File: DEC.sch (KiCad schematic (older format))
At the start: 4 parts

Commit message: wiring
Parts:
- gave numbers to parts that had none: 4
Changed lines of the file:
@@
 $Descr A4 11693 8268
 encoding utf-8
-Sheet 8 8
+Sheet 8 20
 Title ""
 Date ""
@@
 Z7
 $Comp
-L 74LS283 U?
+L 74LS283 U11
 U 1 1 5AE75C93
 P 3050 4250
-F 0 "U?" H 3050 4250 50  0000 C CNN
+F 0 "U11" H 3050 4250 50  0000 C CNN
 F 1 "74LS283" H 3100 3900 50  0000 C CNN
 F 2 "" H 3050 4250 50  0000 C CNN
@@
 $EndComp
 $Comp
-L 74LS283 U?
+L 74LS283 U12
 U 1 1 5AE75D41
 P 4625 4350
-F 0 "U?" H 4625 4350 50  0000 C CNN
+F 0 "U12" H 4625 4350 50  0000 C CNN
 F 1 "74LS283" H 4675 4000 50  0000 C CNN
 F 2 "" H 4625 4350 50  0000 C CNN
@@
 	4625 3100 4625 3650
 $Comp
-L VCC #PWR?
+L VCC #PWR14
 U 1 1 5AE760F6
 P 3375 5400
-F 0 "#PWR?" H 3375 5250 50  0001 C CNN
+F 0 "#PWR14" H 3375 5250 50  0001 C CNN
 F 1 "VCC" H 3375 5550 50  0000 C CNN
 F 2 "" H 3375 5400 50  0000 C CNN
@@
 $EndComp
 $Comp
-L VCC #PWR?
+L VCC #PWR15
 U 1 1 5AE7610E
 P 5025 5400
-F 0 "#PWR?" H 5025 5250 50  0001 C CNN
+F 0 "#PWR15" H 5025 5250 50  0001 C CNN
 F 1 "VCC" H 5025 5550 50  0000 C CNN
 F 2 "" H 5025 5400 50  0000 C CNN
@@
 	5075 5050 4975 5050
 $Comp
-L VCC #PWR?
+L VCC #PWR13
 U 1 1 5AE7639B
 P 2075 3750
-F 0 "#PWR?" H 2075 3600 50  0001 C CNN
+F 0 "#PWR13" H 2075 3600 50  0001 C CNN
 F 1 "VCC" H 2075 3900 50  0000 C CNN
 F 2 "" H 2075 3750 50  0000 C CNN
@@
 $EndComp
 $Comp
-L GND #PWR?
+L GND #PWR12
 U 1 1 5AE763B3
 P 2050 4500
-F 0 "#PWR?" H 2050 4250 50  0001 C CNN
+F 0 "#PWR12" H 2050 4250 50  0001 C CNN
 F 1 "GND" H 2050 4350 50  0000 C CNN
 F 2 "" H 2050 4500 50  0000 C CNN
@@
 $EndComp
 $Comp
-L GND #PWR?
+L GND #PWR16
 U 1 1 5AE763CB
 P 5600 3900
-F 0 "#PWR?" H 5600 3650 50  0001 C CNN
+F 0 "#PWR16" H 5600 3650 50  0001 C CNN
 F 1 "GND" H 5600 3750 50  0000 C CNN
 F 2 "" H 5600 3900 50  0000 C CNN
@@
 	2400 4950 2600 4950
 $Comp
-L C_Small C?
+L C_Small C5
 U 1 1 5AE7641F
 P 2025 4075
-F 0 "C?" H 2035 4145 50  0000 L CNN
+F 0 "C5" H 2035 4145 50  0000 L CNN
 F 1 "100n" H 2035 3995 50  0000 L CNN
 F 2 "" H 2025 4075 50  0000 C CNN
@@
 $EndComp
 $Comp
-L C_Small C?
+L C_Small C6
 U 1 1 5AE76480
 P 5375 4375
-F 0 "C?" H 5385 4445 50  0000 L CNN
+F 0 "C6" H 5385 4445 50  0000 L CNN
 F 1 "100n" H 5385 4295 50  0000 L CNN
 F 2 "" H 5375 4375 50  0000 C CNN

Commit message: SPICE capacitance and ground symbols
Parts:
- removed C5, C6: 100n, symbol C_Small
- added C? (x2): C, symbol C
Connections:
- net labels added: 0
- net labels removed: GND
- wire segments 58 -> 61
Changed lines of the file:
@@
 EESchema Schematic File Version 2
-LIBS:power
-LIBS:device
-LIBS:transistors
-LIBS:conn
-LIBS:linear
-LIBS:regul
-LIBS:74xx
-LIBS:cmos4000
-LIBS:adc-dac
-LIBS:memory
-LIBS:xilinx
-LIBS:microcontrollers
-LIBS:dsp
-LIBS:microchip
-LIBS:analog_switches
-LIBS:motorola
-LIBS:texas
-LIBS:intel
-LIBS:audio
-LIBS:interface
-LIBS:digital-audio
-LIBS:philips
-LIBS:display
-LIBS:cypress
-LIBS:siliconi
-LIBS:opto
-LIBS:atmel
-LIBS:contrib
-LIBS:valves
+LIBS:spice
+LIBS:pspice
 LIBS:myCpu-cache
 EELAYER 25 0
@@
 L VCC #PWR15
 U 1 1 5AE7610E
-P 5025 5400
-F 0 "#PWR15" H 5025 5250 50  0001 C CNN
-F 1 "VCC" H 5025 5550 50  0000 C CNN
-F 2 "" H 5025 5400 50  0000 C CNN
-F 3 "" H 5025 5400 50  0000 C CNN
-	1    5025 5400
+P 4925 5400
+F 0 "#PWR15" H 4925 5250 50  0001 C CNN
+F 1 "VCC" H 4925 5550 50  0000 C CNN
+F 2 "" H 4925 5400 50  0000 C CNN
+F 3 "" H 4925 5400 50  0000 C CNN
+	1    4925 5400
 	1    0    0    -1
 $EndComp
@@
 	3200 5400 3200 4950
 Wire Wire Line
-	3200 4950 3500 4950
+	3200 4950 3300 4950
+Wire Wire Line
+	3300 4950 3400 4950
+Wire Wire Line
+	3400 4950 3500 4950
 Connection ~ 3300 4950
 Connection ~ 3400 4950
 Wire Wire Line
-	4775 5050 5025 5050
+	4775 5050 4875 5050
+Wire Wire Line
+	4875 5050 4975 5050
+Wire Wire Line
+	4975 5050 5025 5050
 Connection ~ 4875 5050
-Wire Wire Line
-	5025 5050 5025 5400
 Connection ~ 4975 5050
 Wire Wire Line
@@
 	1    0    0    -1
 $EndComp
-$Comp
-L GND #PWR12
-U 1 1 5AE763B3
-P 2050 4500
-F 0 "#PWR12" H 2050 4250 50  0001 C CNN
-F 1 "GND" H 2050 4350 50  0000 C CNN
-F 2 "" H 2050 4500 50  0000 C CNN
-F 3 "" H 2050 4500 50  0000 C CNN
-	1    2050 4500
-	1    0    0    -1
-$EndComp
-$Comp
-L GND #PWR16
-U 1 1 5AE763CB
-P 5600 3900
-F 0 "#PWR16" H 5600 3650 50  0001 C CNN
-F 1 "GND" H 5600 3750 50  0000 C CNN
-F 2 "" H 5600 3900 50  0000 C CNN
-F 3 "" H 5600 3900 50  0000 C CNN
-	1    5600 3900
-	1    0    0    -1
-$EndComp
-Wire Wire Line
-	2025 4500 2400 4500
 Wire Wire Line
 	2400 4500 2400 4950
@@
 	2400 4950 2600 4950
 $Comp
-L C_Small C5
-U 1 1 5AE7641F
-P 2025 4075
-F 0 "C5" H 2035 4145 50  0000 L CNN
-F 1 "100n" H 2035 3995 50  0000 L CNN
-F 2 "" H 2025 4075 50  0000 C CNN
-F 3 "" H 2025 4075 50  0000 C CNN
-	1    2025 4075
-	1    0    0    -1
-$EndComp
-$Comp
-L C_Small C6
-U 1 1 5AE76480
-P 5375 4375
-F 0 "C6" H 5385 4445 50  0000 L CNN
-F 1 "100n" H 5385 4295 50  0000 L CNN
-F 2 "" H 5375 4375 50  0000 C CNN
-F 3 "" H 5375 4375 50  0000 C CNN
-	1    5375 4375
-	1    0    0    -1
-$EndComp
-Wire Wire Line
-	2075 3750 2075 3975
-Wire Wire Line
-	2075 3975 2025 3975
-Wire Wire Line
-	2025 4175 2025 4500
-Connection ~ 2050 4500
-Wire Wire Line
-	5375 4475 5375 5400
-Wire Wire Line
-	5375 5400 5025 5400
-Wire Wire Line
-	5375 4275 5425 4275
-Wire Wire Line
-	5425 4275 5425 3900
-Wire Wire Line
-	5425 3900 5600 3900
+L C C?
+U 1 1 5AEBFB4F
+P 2075 4000
+F 0 "C?" V 1925 4000 60  0000 C CNN
+F 1 "C" V 2225 4000 60  0000 C CNN
+F 2 "" H 2075 4000 60  0000 C CNN
+F 3 "" H 2075 4000 60  0000 C CNN
+	1    2075 4000
+	1    0    0    -1
+$EndComp
+$Comp
+L C C?
+U 1 1 5AEBFBCE
+P 5475 5100
+F 0 "C?" V 5325 5100 60  0000 C CNN
+F 1 "C" V 5625 5100 60  0000 C CNN
+F 2 "" H 5475 5100 60  0000 C CNN
+F 3 "" H 5475 5100 60  0000 C CNN
+	1    5475 5100
+	1    0    0    -1
+$EndComp
+$Comp
+L 0 #GND?
+U 1 1 5AEBFC3B
+P 5500 4525
+F 0 "#GND?" H 5500 4425 60  0001 C CNN
+F 1 "0" H 5500 4455 60  0000 C CNN
+F 2 "" H 5500 4525 60  0000 C CNN
+F 3 "" H 5500 4525 60  0000 C CNN
+	1    5500 4525
+	1    0    0    -1
+$EndComp
+$Comp
+L 0 #GND?
+U 1 1 5AEBFC57
+P 2125 4525
+F 0 "#GND?" H 2125 4425 60  0001 C CNN
+F 1 "0" H 2125 4455 60  0000 C CNN
+F 2 "" H 2125 4525 60  0000 C CNN
+F 3 "" H 2125 4525 60  0000 C CNN
+	1    2125 4525
+	1    0    0    -1
+$EndComp
+Wire Wire Line
+	2075 4250 2075 4525
+Wire Wire Line
+	2075 4525 2125 4525
+Wire Wire Line
+	2400 4500 2125 4500
+Wire Wire Line
+	2125 4500 2125 4525
+Wire Wire Line
+	5475 4850 5475 4525
+Wire Wire Line
+	5475 4525 5500 4525
+Wire Wire Line
+	5025 5075 4925 5400
+Wire Wire Line
+	4925 5400 5475 5400
+Wire Wire Line
+	5475 5400 5475 5350
 $EndSCHEMATC

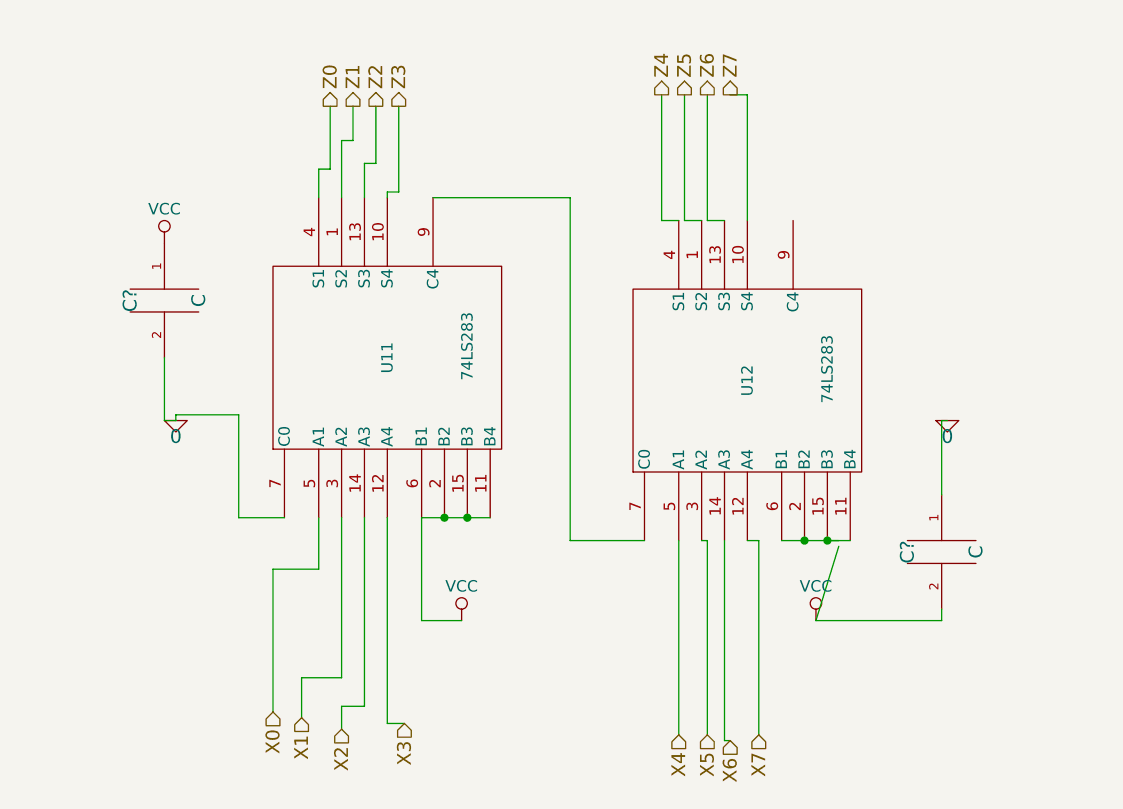
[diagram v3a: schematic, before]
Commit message: fixed duplicate names
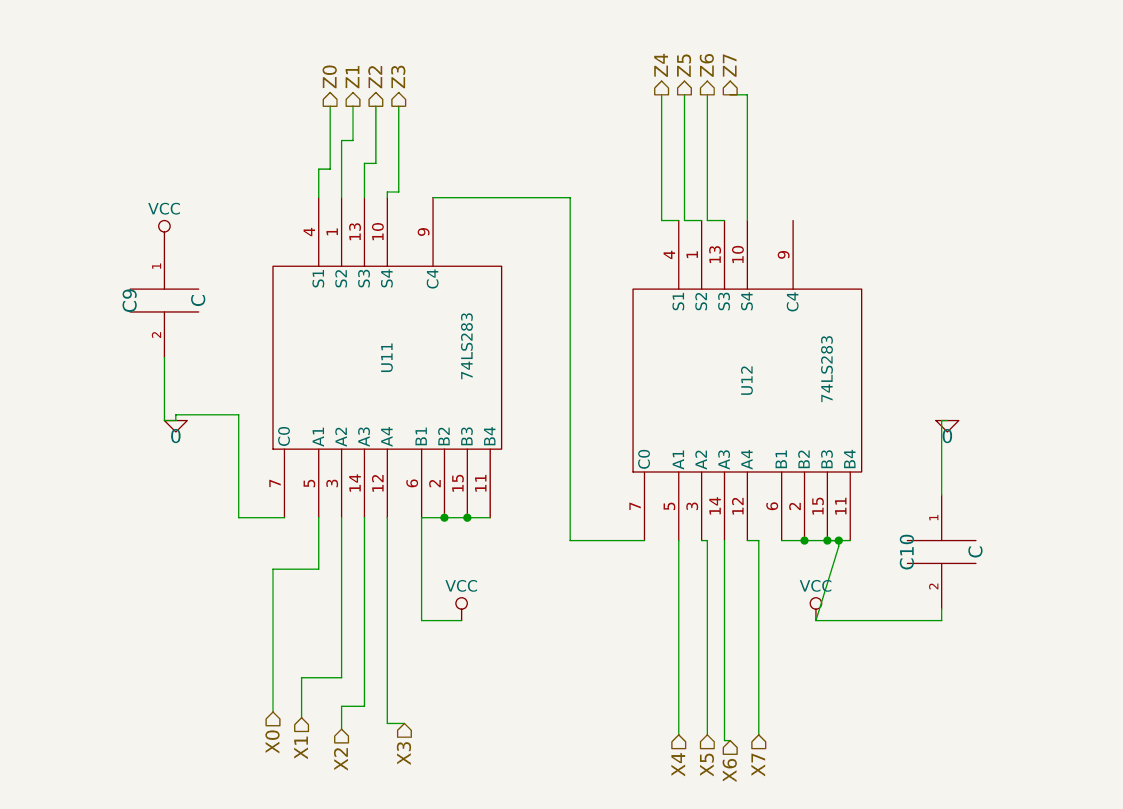
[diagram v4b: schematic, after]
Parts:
- gave numbers to parts that had none: 2
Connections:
- wire segments 61 -> 58
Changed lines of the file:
@@
 	4625 3100 4625 3650
 $Comp
-L VCC #PWR14
+L VCC #PWR010
 U 1 1 5AE760F6
 P 3375 5400
-F 0 "#PWR14" H 3375 5250 50  0001 C CNN
+F 0 "#PWR010" H 3375 5250 50  0001 C CNN
 F 1 "VCC" H 3375 5550 50  0000 C CNN
 F 2 "" H 3375 5400 50  0000 C CNN
@@
 $EndComp
 $Comp
-L VCC #PWR15
+L VCC #PWR011
 U 1 1 5AE7610E
 P 4925 5400
-F 0 "#PWR15" H 4925 5250 50  0001 C CNN
+F 0 "#PWR011" H 4925 5250 50  0001 C CNN
 F 1 "VCC" H 4925 5550 50  0000 C CNN
 F 2 "" H 4925 5400 50  0000 C CNN
@@
 	3200 5400 3200 4950
 Wire Wire Line
-	3200 4950 3300 4950
-Wire Wire Line
-	3300 4950 3400 4950
-Wire Wire Line
-	3400 4950 3500 4950
+	3200 4950 3500 4950
 Connection ~ 3300 4950
 Connection ~ 3400 4950
 Wire Wire Line
-	4775 5050 4875 5050
-Wire Wire Line
-	4875 5050 4975 5050
-Wire Wire Line
-	4975 5050 5025 5050
+	4775 5050 5025 5050
 Connection ~ 4875 5050
 Connection ~ 4975 5050
@@
 	5075 5050 4975 5050
 $Comp
-L VCC #PWR13
+L VCC #PWR012
 U 1 1 5AE7639B
 P 2075 3750
-F 0 "#PWR13" H 2075 3600 50  0001 C CNN
+F 0 "#PWR012" H 2075 3600 50  0001 C CNN
 F 1 "VCC" H 2075 3900 50  0000 C CNN
 F 2 "" H 2075 3750 50  0000 C CNN
@@
 	2400 4950 2600 4950
 $Comp
-L C C?
+L C C9
 U 1 1 5AEBFB4F
 P 2075 4000
-F 0 "C?" V 1925 4000 60  0000 C CNN
+F 0 "C9" V 1925 4000 60  0000 C CNN
 F 1 "C" V 2225 4000 60  0000 C CNN
 F 2 "" H 2075 4000 60  0000 C CNN
@@
 $EndComp
 $Comp
-L C C?
+L C C10
 U 1 1 5AEBFBCE
 P 5475 5100
-F 0 "C?" V 5325 5100 60  0000 C CNN
+F 0 "C10" V 5325 5100 60  0000 C CNN
 F 1 "C" V 5625 5100 60  0000 C CNN
 F 2 "" H 5475 5100 60  0000 C CNN
@@
 $EndComp
 $Comp
-L 0 #GND?
+L 0 #GND12
 U 1 1 5AEBFC3B
 P 5500 4525
-F 0 "#GND?" H 5500 4425 60  0001 C CNN
+F 0 "#GND12" H 5500 4425 60  0001 C CNN
 F 1 "0" H 5500 4455 60  0000 C CNN
 F 2 "" H 5500 4525 60  0000 C CNN
@@
 $EndComp
 $Comp
-L 0 #GND?
+L 0 #GND11
 U 1 1 5AEBFC57
 P 2125 4525
-F 0 "#GND?" H 2125 4425 60  0001 C CNN
+F 0 "#GND11" H 2125 4425 60  0001 C CNN
 F 1 "0" H 2125 4455 60  0000 C CNN
 F 2 "" H 2125 4525 60  0000 C CNN
@@
 Wire Wire Line
 	5475 5400 5475 5350
+Wire Wire Line
+	5025 5050 5025 5075
+Connection ~ 5025 5050
 $EndSCHEMATC

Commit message: NC-symbols
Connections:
- net C_OUT: now reaches U12.9 (C4)
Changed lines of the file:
@@
 	5025 5050 5025 5075
 Connection ~ 5025 5050
+Text HLabel 4975 3175 1    60   Output ~ 0
+C_OUT
+Wire Wire Line
+	4825 3625 4975 3625
+Wire Wire Line
+	4975 3625 4975 3175
+Wire Wire Line
+	4825 3625 4825 3650
 $EndSCHEMATC

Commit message: spice libs from the internet, opened with new kicad 5.0.0, added spice models to components
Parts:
- C10, C9: value C -> 100nF; symbol C -> spice:C
- U11: symbol 74LS283 -> myCpu-rescue:74LS283
- U12: symbol 74LS283 -> myCpu-rescue:74LS283; Spice_Lib_File (none) -> 74hc.lib; Spice_Model (none) -> 74HC283; Spice_Netlist_Enabled (none) -> Y; Spice_Primitive (none) -> X
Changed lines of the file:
@@
-EESchema Schematic File Version 2
-LIBS:spice
-LIBS:pspice
+EESchema Schematic File Version 4
 LIBS:myCpu-cache
-EELAYER 25 0
+EELAYER 26 0
 EELAYER END
 $Descr A4 11693 8268
@@
 Z7
 $Comp
-L 74LS283 U11
+L myCpu-rescue:74LS283 U11
 U 1 1 5AE75C93
 P 3050 4250
@@
 $EndComp
 $Comp
-L 74LS283 U12
+L myCpu-rescue:74LS283 U12
 U 1 1 5AE75D41
 P 4625 4350
@@
 F 2 "" H 4625 4350 50  0000 C CNN
 F 3 "" H 4625 4350 50  0000 C CNN
+F 4 "X" H 4625 4350 50  0001 C CNN "Spice_Primitive"
+F 5 "74HC283" H 4625 4350 50  0001 C CNN "Spice_Model"
+F 6 "Y" H 4625 4350 50  0001 C CNN "Spice_Netlist_Enabled"
+F 7 "74hc.lib" H 4625 4350 50  0001 C CNN "Spice_Lib_File"
 	1    4625 4350
 	0    -1   -1   0
@@
 	4625 3100 4625 3650
 $Comp
-L VCC #PWR010
+L myCpu-rescue:VCC #PWR010
 U 1 1 5AE760F6
 P 3375 5400
@@
 $EndComp
 $Comp
-L VCC #PWR011
+L myCpu-rescue:VCC #PWR011
 U 1 1 5AE7610E
 P 4925 5400
@@
 	3200 5400 3200 4950
 Wire Wire Line
-	3200 4950 3500 4950
+	3200 4950 3300 4950
 Connection ~ 3300 4950
 Connection ~ 3400 4950
 Wire Wire Line
-	4775 5050 5025 5050
+	4775 5050 4875 5050
 Connection ~ 4875 5050
 Connection ~ 4975 5050
 Wire Wire Line
-	5075 5050 4975 5050
-$Comp
-L VCC #PWR012
+	5075 5050 5025 5050
+$Comp
+L myCpu-rescue:VCC #PWR012
 U 1 1 5AE7639B
 P 2075 3750
@@
 	2400 4950 2600 4950
 $Comp
-L C C9
+L spice:C C9
 U 1 1 5AEBFB4F
 P 2075 4000
 F 0 "C9" V 1925 4000 60  0000 C CNN
-F 1 "C" V 2225 4000 60  0000 C CNN
+F 1 "100nF" V 2225 4000 60  0000 C CNN
 F 2 "" H 2075 4000 60  0000 C CNN
 F 3 "" H 2075 4000 60  0000 C CNN
@@
 $EndComp
 $Comp
-L C C10
+L spice:C C10
 U 1 1 5AEBFBCE
 P 5475 5100
 F 0 "C10" V 5325 5100 60  0000 C CNN
-F 1 "C" V 5625 5100 60  0000 C CNN
+F 1 "100nF" V 5625 5100 60  0000 C CNN
 F 2 "" H 5475 5100 60  0000 C CNN
 F 3 "" H 5475 5100 60  0000 C CNN
@@
 $EndComp
 $Comp
-L 0 #GND12
+L spice:0 #GND12
 U 1 1 5AEBFC3B
 P 5500 4525
@@
 $EndComp
 $Comp
-L 0 #GND11
+L spice:0 #GND11
 U 1 1 5AEBFC57
 P 2125 4525
@@
 Wire Wire Line
 	4825 3625 4825 3650
+Wire Wire Line
+	3300 4950 3400 4950
+Wire Wire Line
+	3400 4950 3500 4950
+Wire Wire Line
+	4875 5050 4975 5050
+Wire Wire Line
+	4975 5050 5025 5050
 $EndSCHEMATC

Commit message: lots of work done
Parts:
- renumbered C9 to C10, C10 to C11, U11 to U12, U12 to U13
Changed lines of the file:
@@
 $Descr A4 11693 8268
 encoding utf-8
-Sheet 8 21
+Sheet 8 81
 Title ""
 Date ""
@@
 Z7
 $Comp
-L myCpu-rescue:74LS283 U11
+L myCpu-rescue:74LS283 U12
 U 1 1 5AE75C93
 P 3050 4250
-F 0 "U11" H 3050 4250 50  0000 C CNN
+F 0 "U12" H 3050 4250 50  0000 C CNN
 F 1 "74LS283" H 3100 3900 50  0000 C CNN
 F 2 "" H 3050 4250 50  0000 C CNN
@@
 $EndComp
 $Comp
-L myCpu-rescue:74LS283 U12
+L myCpu-rescue:74LS283 U13
 U 1 1 5AE75D41
 P 4625 4350
-F 0 "U12" H 4625 4350 50  0000 C CNN
+F 0 "U13" H 4625 4350 50  0000 C CNN
 F 1 "74LS283" H 4675 4000 50  0000 C CNN
 F 2 "" H 4625 4350 50  0000 C CNN
@@
 	4625 3100 4625 3650
 $Comp
-L myCpu-rescue:VCC #PWR010
+L myCpu-rescue:VCC #PWR015
 U 1 1 5AE760F6
 P 3375 5400
-F 0 "#PWR010" H 3375 5250 50  0001 C CNN
+F 0 "#PWR015" H 3375 5250 50  0001 C CNN
 F 1 "VCC" H 3375 5550 50  0000 C CNN
 F 2 "" H 3375 5400 50  0000 C CNN
@@
 $EndComp
 $Comp
-L myCpu-rescue:VCC #PWR011
+L myCpu-rescue:VCC #PWR016
 U 1 1 5AE7610E
 P 4925 5400
-F 0 "#PWR011" H 4925 5250 50  0001 C CNN
+F 0 "#PWR016" H 4925 5250 50  0001 C CNN
 F 1 "VCC" H 4925 5550 50  0000 C CNN
 F 2 "" H 4925 5400 50  0000 C CNN
@@
 	5075 5050 5025 5050
 $Comp
-L myCpu-rescue:VCC #PWR012
+L myCpu-rescue:VCC #PWR014
 U 1 1 5AE7639B
 P 2075 3750
-F 0 "#PWR012" H 2075 3600 50  0001 C CNN
+F 0 "#PWR014" H 2075 3600 50  0001 C CNN
 F 1 "VCC" H 2075 3900 50  0000 C CNN
 F 2 "" H 2075 3750 50  0000 C CNN
@@
 	2400 4950 2600 4950
 $Comp
-L spice:C C9
+L spice:C C10
 U 1 1 5AEBFB4F
 P 2075 4000
-F 0 "C9" V 1925 4000 60  0000 C CNN
+F 0 "C10" V 1925 4000 60  0000 C CNN
 F 1 "100nF" V 2225 4000 60  0000 C CNN
 F 2 "" H 2075 4000 60  0000 C CNN
@@
 $EndComp
 $Comp
-L spice:C C10
+L spice:C C11
 U 1 1 5AEBFBCE
 P 5475 5100
-F 0 "C10" V 5325 5100 60  0000 C CNN
+F 0 "C11" V 5325 5100 60  0000 C CNN
 F 1 "100nF" V 5625 5100 60  0000 C CNN
 F 2 "" H 5475 5100 60  0000 C CNN
@@
 $EndComp
 $Comp
-L spice:0 #GND12
+L spice:0 #GND17
 U 1 1 5AEBFC3B
 P 5500 4525
-F 0 "#GND12" H 5500 4425 60  0001 C CNN
+F 0 "#GND17" H 5500 4425 60  0001 C CNN
 F 1 "0" H 5500 4455 60  0000 C CNN
 F 2 "" H 5500 4525 60  0000 C CNN
@@
 $EndComp
 $Comp
-L spice:0 #GND11
+L spice:0 #GND16
 U 1 1 5AEBFC57
 P 2125 4525
-F 0 "#GND11" H 2125 4425 60  0001 C CNN
+F 0 "#GND16" H 2125 4425 60  0001 C CNN
 F 1 "0" H 2125 4455 60  0000 C CNN
 F 2 "" H 2125 4525 60  0000 C CNN
